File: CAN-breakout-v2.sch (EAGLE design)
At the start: 10 parts, among them IC1 TJA1049

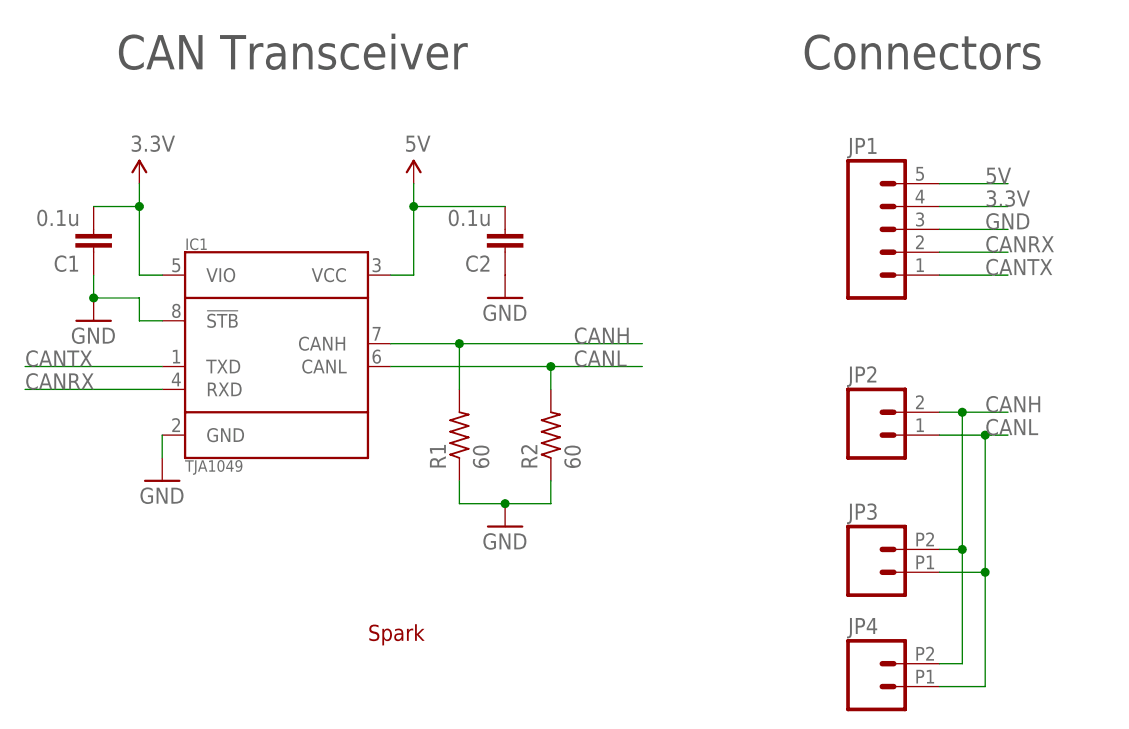
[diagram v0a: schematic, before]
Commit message: Fix the termination
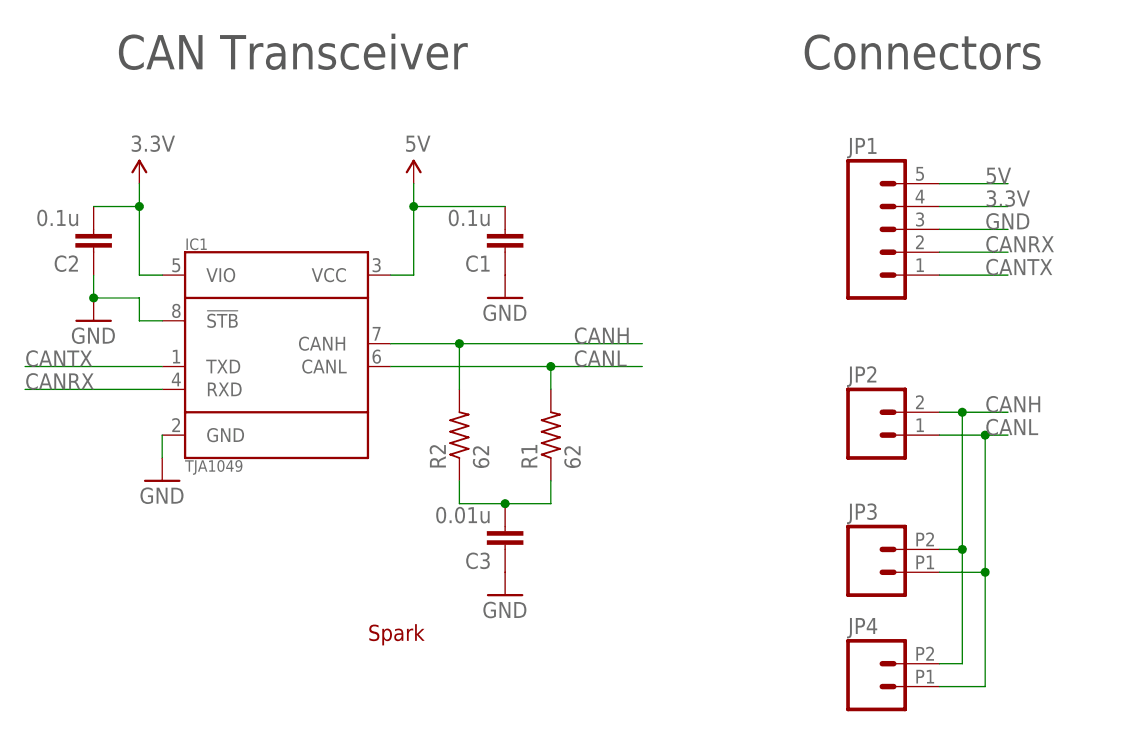
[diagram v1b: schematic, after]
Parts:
- added C3: 0.01u, rcl:C-EUC1206
- C1, C2: PARTNO GRM155R71C104KA88D -> 12065C104KAT2A
- R1: value 60 -> 62; PARTNO ERJ-2RKF6202X -> RC1206FR-0762RL
- R2: value 60 -> 62; PARTNO ERJ-2RKF1002X -> RC1206FR-0762RL
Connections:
- new net N$7: C3.2, R1.1, R2.1
- net 3.3V: now also C2.2; no longer C1.2
- net 5V: now also C1.2; no longer C2.2
- net CANH: now also R2.2; no longer R1.2
- net CANL: now also R1.2; no longer R2.2
- net GND: now also C3.1; no longer R1.1, R2.1
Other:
- moved on the sheet: C1, C2, R1, R2
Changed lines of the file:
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@@
 <parts>
 <part name="U$2" library="SparkFun-Aesthetics" deviceset="5V" device=""/>
-<part name="C2" library="rcl" deviceset="C-EU" device="C1206" value="0.1u">
-<attribute name="PARTNO" value="GRM155R71C104KA88D"/>
+<part name="C1" library="rcl" deviceset="C-EU" device="C1206" value="0.1u">
+<attribute name="PARTNO" value="12065C104KAT2A"/>
 </part>
 <part name="GND6" library="SparkFun-Aesthetics" deviceset="GND" device=""/>
@@
 <attribute name="PARTNO" value="TJA1049T-118"/>
 </part>
-<part name="R1" library="rcl" deviceset="R-US_" device="R1206" value="60">
-<attribute name="PARTNO" value="ERJ-2RKF6202X"/>
-</part>
-<part name="R2" library="rcl" deviceset="R-US_" device="R1206" value="60">
-<attribute name="PARTNO" value="ERJ-2RKF1002X"/>
-</part>
-<part name="C1" library="rcl" deviceset="C-EU" device="C1206" value="0.1u">
-<attribute name="PARTNO" value="GRM155R71C104KA88D"/>
+<part name="R2" library="rcl" deviceset="R-US_" device="R1206" value="62">
+<attribute name="PARTNO" value="RC1206FR-0762RL"/>
+</part>
+<part name="R1" library="rcl" deviceset="R-US_" device="R1206" value="62">
+<attribute name="PARTNO" value="RC1206FR-0762RL"/>
+</part>
+<part name="C2" library="rcl" deviceset="C-EU" device="C1206" value="0.1u">
+<attribute name="PARTNO" value="12065C104KAT2A"/>
 </part>
 <part name="GND1" library="SparkFun-Aesthetics" deviceset="GND" device=""/>
@@
 <part name="U$3" library="Spark" deviceset="SPARK_LOGO2" device="">
 <attribute name="BOM" value="EXCLUDE"/>
+</part>
+<part name="C3" library="rcl" deviceset="C-EU" device="C1206" value="0.01u">
+<attribute name="PARTNO" value="12065C103KAT2A"/>
 </part>
 </parts>
@@
 <instances>
 <instance part="U$2" gate="G$1" x="106.68" y="142.24"/>
-<instance part="C2" gate="G$1" x="116.84" y="134.62" rot="R180">
+<instance part="C1" gate="G$1" x="116.84" y="134.62" rot="R180">
 <attribute name="PARTNO" x="116.84" y="134.62" size="1.778" layer="96" rot="R90" display="off"/>
 </instance>
@@
 <attribute name="PARTNO" x="91.44" y="116.84" size="1.778" layer="96" display="off"/>
 </instance>
-<instance part="R1" gate="G$1" x="111.76" y="114.3" rot="R90">
+<instance part="R2" gate="G$1" x="111.76" y="114.3" rot="R90">
 <attribute name="PARTNO" x="111.76" y="114.3" size="1.778" layer="96" display="off"/>
 </instance>
-<instance part="R2" gate="G$1" x="121.92" y="114.3" rot="R90">
+<instance part="R1" gate="G$1" x="121.92" y="114.3" rot="R90">
 <attribute name="PARTNO" x="121.92" y="114.3" size="1.778" layer="96" display="off"/>
 </instance>
-<instance part="C1" gate="G$1" x="71.12" y="134.62" rot="R180">
+<instance part="C2" gate="G$1" x="71.12" y="134.62" rot="R180">
 <attribute name="PARTNO" x="71.12" y="134.62" size="1.778" layer="96" rot="R90" display="off"/>
 </instance>
 <instance part="GND1" gate="1" x="71.12" y="127"/>
-<instance part="GND2" gate="1" x="116.84" y="104.14"/>
+<instance part="GND2" gate="1" x="116.84" y="96.52"/>
 <instance part="JP1" gate="G$1" x="157.48" y="137.16">
 <attribute name="PARTNO" x="157.48" y="137.16" size="1.778" layer="96" display="off"/>
@@
 <instance part="U$3" gate="G$1" x="101.6" y="91.44">
 <attribute name="BOM" x="101.6" y="91.44" size="1.778" layer="96" display="off"/>
+</instance>
+<instance part="C3" gate="G$1" x="116.84" y="101.6" rot="R180">
+<attribute name="PARTNO" x="116.84" y="101.6" size="1.778" layer="96" rot="R90" display="off"/>
 </instance>
 </instances>
@@
 <net name="GND" class="0">
 <segment>
-<pinref part="C2" gate="G$1" pin="1"/>
+<pinref part="C1" gate="G$1" pin="1"/>
 <pinref part="GND6" gate="1" pin="GND"/>
 </segment>
@@
 </segment>
 <segment>
-<pinref part="C1" gate="G$1" pin="1"/>
+<pinref part="C2" gate="G$1" pin="1"/>
 <pinref part="GND1" gate="1" pin="GND"/>
 <wire x1="71.12" y1="129.54" x2="71.12" y2="132.08" width="0.1524" layer="91"/>
@@
 </segment>
 <segment>
-<pinref part="R2" gate="G$1" pin="1"/>
-<wire x1="121.92" y1="109.22" x2="121.92" y2="106.68" width="0.1524" layer="91"/>
-<pinref part="R1" gate="G$1" pin="1"/>
-<wire x1="121.92" y1="106.68" x2="116.84" y2="106.68" width="0.1524" layer="91"/>
-<wire x1="116.84" y1="106.68" x2="111.76" y2="106.68" width="0.1524" layer="91"/>
-<wire x1="111.76" y1="106.68" x2="111.76" y2="109.22" width="0.1524" layer="91"/>
-<pinref part="GND2" gate="1" pin="GND"/>
-<junction x="116.84" y="106.68"/>
-</segment>
-<segment>
 <pinref part="JP1" gate="G$1" pin="3"/>
 <wire x1="165.1" y1="137.16" x2="172.72" y2="137.16" width="0.1524" layer="91"/>
 <label x="170.18" y="137.16" size="1.778" layer="95"/>
+</segment>
+<segment>
+<pinref part="C3" gate="G$1" pin="1"/>
+<pinref part="GND2" gate="1" pin="GND"/>
 </segment>
 </net>
@@
 <pinref part="U$2" gate="G$1" pin="5V"/>
 <wire x1="106.68" y1="132.08" x2="106.68" y2="139.7" width="0.1524" layer="91"/>
-<pinref part="C2" gate="G$1" pin="2"/>
+<pinref part="C1" gate="G$1" pin="2"/>
 <wire x1="106.68" y1="139.7" x2="106.68" y2="142.24" width="0.1524" layer="91"/>
 <wire x1="116.84" y1="139.7" x2="106.68" y2="139.7" width="0.1524" layer="91"/>
@@
 <pinref part="P+6" gate="G$1" pin="3.3V"/>
 <wire x1="76.2" y1="132.08" x2="76.2" y2="139.7" width="0.1524" layer="91"/>
-<pinref part="C1" gate="G$1" pin="2"/>
+<pinref part="C2" gate="G$1" pin="2"/>
 <wire x1="76.2" y1="139.7" x2="76.2" y2="142.24" width="0.1524" layer="91"/>
 <wire x1="71.12" y1="139.7" x2="76.2" y2="139.7" width="0.1524" layer="91"/>
@@
 <pinref part="IC1" gate="G$1" pin="CANH"/>
 <wire x1="104.14" y1="124.46" x2="111.76" y2="124.46" width="0.1524" layer="91"/>
-<pinref part="R1" gate="G$1" pin="2"/>
+<pinref part="R2" gate="G$1" pin="2"/>
 <wire x1="111.76" y1="124.46" x2="132.08" y2="124.46" width="0.1524" layer="91"/>
 <wire x1="111.76" y1="119.38" x2="111.76" y2="124.46" width="0.1524" layer="91"/>
@@
 <pinref part="IC1" gate="G$1" pin="CANL"/>
 <wire x1="104.14" y1="121.92" x2="121.92" y2="121.92" width="0.1524" layer="91"/>
-<pinref part="R2" gate="G$1" pin="2"/>
+<pinref part="R1" gate="G$1" pin="2"/>
 <wire x1="121.92" y1="121.92" x2="132.08" y2="121.92" width="0.1524" layer="91"/>
 <wire x1="121.92" y1="119.38" x2="121.92" y2="121.92" width="0.1524" layer="91"/>
@@
 </segment>
 </net>
+<net name="N$7" class="0">
+<segment>
+<pinref part="R1" gate="G$1" pin="1"/>
+<wire x1="121.92" y1="109.22" x2="121.92" y2="106.68" width="0.1524" layer="91"/>
+<pinref part="C3" gate="G$1" pin="2"/>
+<wire x1="116.84" y1="106.68" x2="121.92" y2="106.68" width="0.1524" layer="91"/>
+<pinref part="R2" gate="G$1" pin="1"/>
+<wire x1="111.76" y1="106.68" x2="111.76" y2="109.22" width="0.1524" layer="91"/>
+<wire x1="116.84" y1="106.68" x2="111.76" y2="106.68" width="0.1524" layer="91"/>
+<junction x="116.84" y="106.68"/>
+</segment>
+</net>
